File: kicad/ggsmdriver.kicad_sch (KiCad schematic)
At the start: 69 parts, among them J1 DC-005, J2 VIN 9-24V, J3 MOTOR A1 A2 B1 B2, J4 EXP, J5 USB-C, SW1 BOOT, SW2 RESET, U1 STM32G0B1CBT6, U2 TMC2209-LA, U3 TPS54202DDCR, U4 XC6206P332MR, U5 USBLC6-2SC6

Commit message: PCB: hand-laid TMC2209 power stage, no VREF trimmer, real track widths
Motor outputs run 1 mm wide straight to J3 next to the chip (J3 now A2 A1 B1 B2),
sense resistors and VS vias sit at the driver pins, VS caps join through a new
In2.Cu VIN plane, as on the Adafruit breakout. VREF goes to GND since current is
always set over UART. Netclass widths now reach the router. Fully routed, no DRC
errors; fab files regenerated.

Co-Authored-By: Claude Opus 5.5 (1M context) <noreply@anthropic.com>
Claude-Session: https://claude.ai/code/session_01VFhb1Qv7mkaGrgvtw2CS4q
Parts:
- removed R11: 33k, Resistor_SMD:R_0603_1608Metric, symbol Device:R
- removed RV1: 10k current, Potentiometer_SMD:Potentiometer_Bourns_3314J_Vertical, symbol Device:R_Potentiometer_Trim
- J3: value MOTOR A1 A2 B1 B2 -> MOTOR A2 A1 B1 B2
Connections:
- net TMC_VREF is gone; now on net GND: U2.17 (VREF)
- net MOT_A1: now also J3.2 (Pin_2); no longer J3.1 (Pin_1)
- net MOT_A2: now also J3.1 (Pin_1); no longer J3.2 (Pin_2)
- net TMC_SPREAD: no longer U2.7 (SPREAD)
- no-connect marks 31 -> 32
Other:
- moved on the sheet: C16, C17, C18, C19, C20, C21, C22, C23, D4, D5, D6, H1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

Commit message: PCB round 2: no barrel jack, power terminal beside motor terminal, stocked parts
J1 removed; the VIN/GND terminal sits right below the motor terminal on the right
edge. TMC2209-LA-T (C2150710), RALEC 50 mOhm 1206 sense resistors (C154645), red
Basic / green LEDs replace out-of-stock parts. SPREAD pin reconnected (lost in the
previous edit). Fully routed, no DRC errors; fab files regenerated.

Co-Authored-By: Claude Opus 5.5 (1M context) <noreply@anthropic.com>
Claude-Session: https://claude.ai/code/session_01VFhb1Qv7mkaGrgvtw2CS4q
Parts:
- removed J1: DC-005, Connector_BarrelJack:BarrelJack_Horizontal, symbol Connector:Barrel_Jack_Switch
- D2: value PWR green -> PWR red; LCSC C12624 -> C2286
- D3: value STATUS blue -> STATUS green; LCSC C72041 -> C12624
- D4: value STEP yellow -> STEP red; LCSC C2287 -> C2286
- J2: value VIN 9-24V -> VIN 9-24V GND
- R10, R9: LCSC C5185600 -> C154645
- U2: value TMC2209-LA -> TMC2209-LA-T; LCSC C465949 -> C2150710
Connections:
- net TMC_SPREAD: now also U2.7 (SPREAD)
- no-connect marks 32 -> 30
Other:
- note removed: "Power input"
- moved on the sheet: C1, C10, C16, C17, C18, C19, C2, C20, C21, C22, C23, C3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

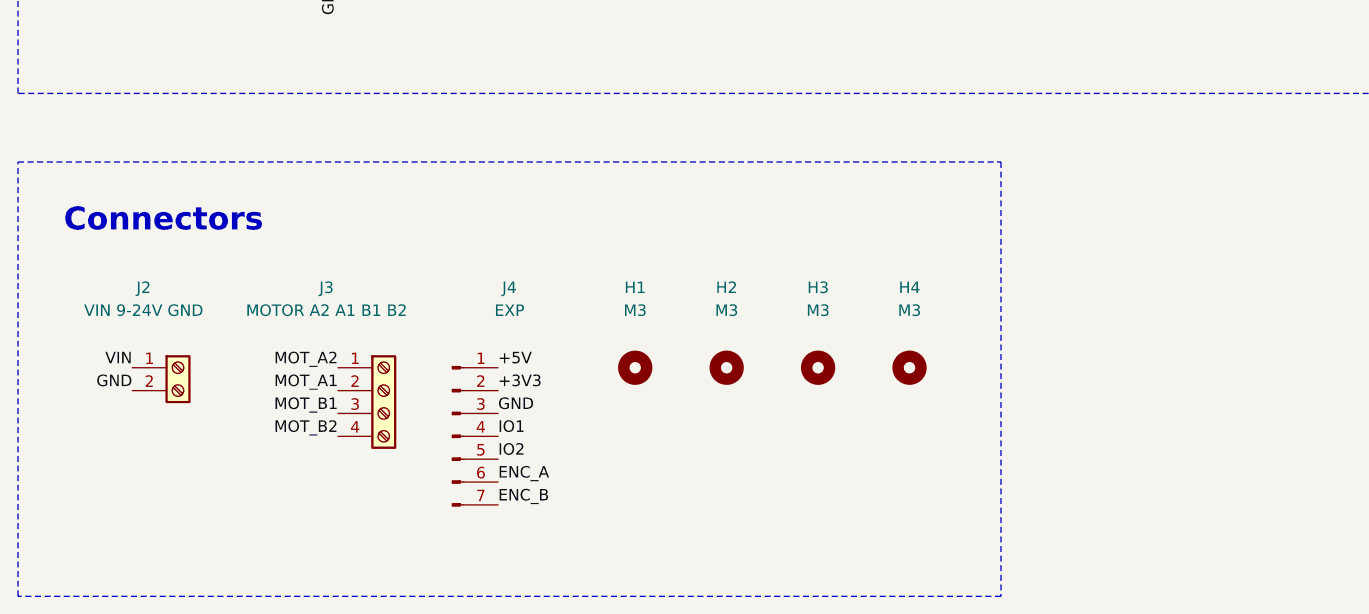
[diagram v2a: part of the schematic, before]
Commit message: PCB: stocked 22 uF cap and three 2-pole terminals
C20 is now Lelon VES220M1HTR-0605 (C176676). The out-of-stock 4-pole motor terminal is
split into two KF350-3.5-2P blocks (J6 coil B, J3 coil A), so power and motor are three
identical 2P blocks along the right edge. Coil B tracks, R10 and C19 moved to make room.
Fully routed, no DRC errors; fab files regenerated.

Co-Authored-By: Claude Opus 5.5 (1M context) <noreply@anthropic.com>
Claude-Session: https://claude.ai/code/session_01VFhb1Qv7mkaGrgvtw2CS4q
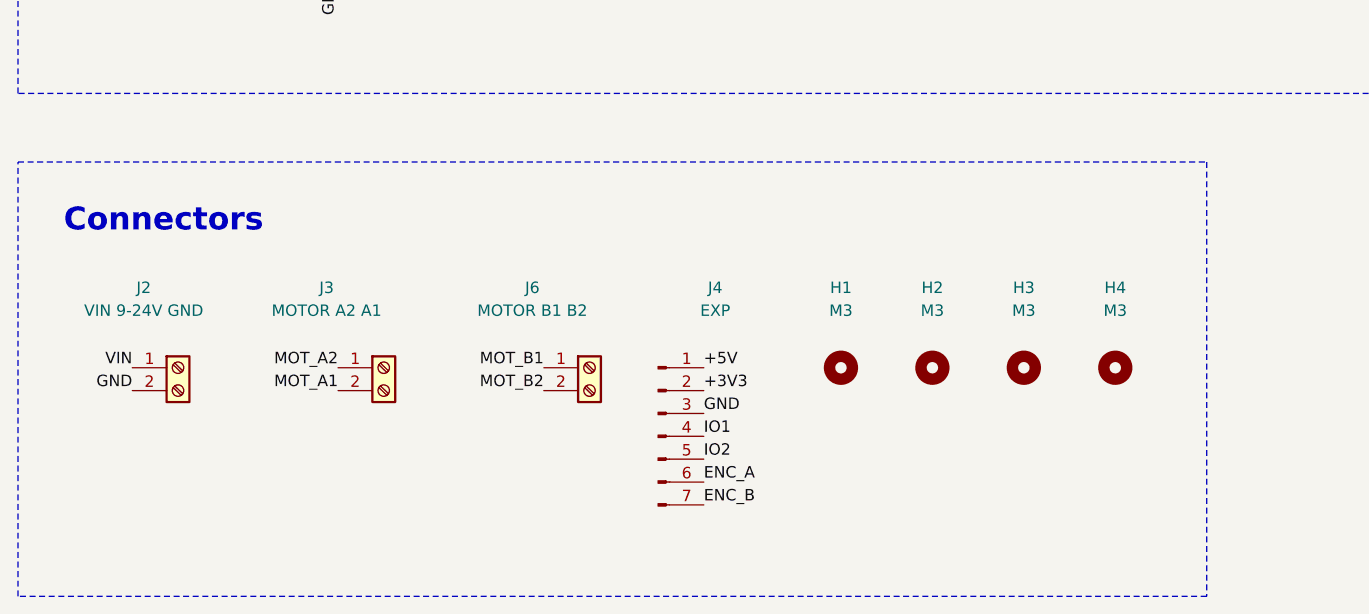
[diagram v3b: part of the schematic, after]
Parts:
- added J6: MOTOR B1 B2, TerminalBlock_Phoenix:TerminalBlock_Phoenix_PT-1,5-2-3.5-H_1x02_P3.50mm_Horizontal, symbol Connector:Screw_Terminal_01x02
- C20: footprint Capacitor_SMD:CP_Elec_6.3x5.9 -> Capacitor_SMD:CP_Elec_6.3x5.4; LCSC C242075 -> C176676
- J3: value MOTOR A2 A1 B1 B2 -> MOTOR A2 A1; footprint TerminalBlock_Phoenix:TerminalBlock_Phoenix_PT-1,5-4-3.5-H_1x04_P3.50mm_Horizontal -> TerminalBlock_Phoenix:TerminalBlock_Phoenix_PT-1,5-2-3.5-H_1x02_P3.50mm_Horizontal; symbol Connector:Screw_Terminal_01x04 -> Connector:Screw_Terminal_01x02; LCSC C42400616 -> C474892
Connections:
- net MOT_B1: now also J6.1 (Pin_1); no longer J3.3 (Pin_3)
- net MOT_B2: now also J6.2 (Pin_2); no longer J3.4 (Pin_4)
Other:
- moved on the sheet: H1, H2, H3, H4, J4
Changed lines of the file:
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@@
   (rectangle
     (start 12.7 246.38)
-    (end 121.92 294.64)
+    (end 144.78 294.64)
     (stroke (width 0) (type dash))
     (fill (type none))
@@
     (property "Reference" "C20" (at 447.04 118.11 0) (effects (font (size 1.27 1.27))))
     (property "Value" "22uF 50V" (at 447.04 120.65 0) (effects (font (size 1.27 1.27))))
-    (property "Footprint" "Capacitor_SMD:CP_Elec_6.3x5.9"
+    (property "Footprint" "Capacitor_SMD:CP_Elec_6.3x5.4"
       (at 447.04 134.62 0)
       (effects (font (size 1.27 1.27)) hide))
     (property "Datasheet" "~" (at 447.04 134.62 0) (effects (font (size 1.27 1.27)) hide))
-    (property "LCSC" "C242075" (at 447.04 134.62 0) (effects (font (size 1.27 1.27)) hide))
+    (property "LCSC" "C176676" (at 447.04 134.62 0) (effects (font (size 1.27 1.27)) hide))
     (pin "1")
     (pin "2")
@@
 )
   (symbol
-    (lib_id "Connector:Screw_Terminal_01x04")
-    (at 53.34 271.78 0)
+    (lib_id "Connector:Screw_Terminal_01x02")
+    (at 53.34 269.24 0)
     (unit 1)
     (in_bom yes)
@@
     (dnp no)
     (property "Reference" "J3" (at 46.99 260.35 0) (effects (font (size 1.27 1.27))))
-    (property "Value" "MOTOR A2 A1 B1 B2" (at 46.99 262.89 0) (effects (font (size 1.27 1.27))))
-    (property "Footprint" "TerminalBlock_Phoenix:TerminalBlock_Phoenix_PT-1,5-4-3.5-H_1x04_P3.50mm_Horizontal"
-      (at 53.34 271.78 0)
-      (effects (font (size 1.27 1.27)) hide))
-    (property "Datasheet" "~" (at 53.34 271.78 0) (effects (font (size 1.27 1.27)) hide))
-    (property "LCSC" "C42400616" (at 53.34 271.78 0) (effects (font (size 1.27 1.27)) hide))
-    (pin "1")
-    (pin "2")
-    (pin "3")
-    (pin "4")
+    (property "Value" "MOTOR A2 A1" (at 46.99 262.89 0) (effects (font (size 1.27 1.27))))
+    (property "Footprint" "TerminalBlock_Phoenix:TerminalBlock_Phoenix_PT-1,5-2-3.5-H_1x02_P3.50mm_Horizontal"
+      (at 53.34 269.24 0)
+      (effects (font (size 1.27 1.27)) hide))
+    (property "Datasheet" "~" (at 53.34 269.24 0) (effects (font (size 1.27 1.27)) hide))
+    (property "LCSC" "C474892" (at 53.34 269.24 0) (effects (font (size 1.27 1.27)) hide))
+    (pin "1")
+    (pin "2")
     (instances
       (project "ggsmdriver"
@@
     (effects (font (size 1.27 1.27)) (justify right bottom))
 )
+  (symbol
+    (lib_id "Connector:Screw_Terminal_01x02")
+    (at 76.2 269.24 0)
+    (unit 1)
+    (in_bom yes)
+    (on_board yes)
+    (dnp no)
+    (property "Reference" "J6" (at 69.85 260.35 0) (effects (font (size 1.27 1.27))))
+    (property "Value" "MOTOR B1 B2" (at 69.85 262.89 0) (effects (font (size 1.27 1.27))))
+    (property "Footprint" "TerminalBlock_Phoenix:TerminalBlock_Phoenix_PT-1,5-2-3.5-H_1x02_P3.50mm_Horizontal"
+      (at 76.2 269.24 0)
+      (effects (font (size 1.27 1.27)) hide))
+    (property "Datasheet" "~" (at 76.2 269.24 0) (effects (font (size 1.27 1.27)) hide))
+    (property "LCSC" "C474892" (at 76.2 269.24 0) (effects (font (size 1.27 1.27)) hide))
+    (pin "1")
+    (pin "2")
+    (instances
+      (project "ggsmdriver"
+        (path "/d2c479e8-b366-5642-b905-795d77a1c823" (reference "J6") (unit 1)))))
   (label "MOT_B1"
-    (at 48.26 274.32 180)
+    (at 71.12 269.24 180)
     (effects (font (size 1.27 1.27)) (justify right bottom))
 )
   (label "MOT_B2"
-    (at 48.26 276.86 180)
+    (at 71.12 271.78 180)
     (effects (font (size 1.27 1.27)) (justify right bottom))
 )
   (symbol
     (lib_id "Connector:Conn_01x07_Pin")
-    (at 60.96 276.86 0)
-    (unit 1)
-    (in_bom yes)
-    (on_board yes)
-    (dnp no)
-    (property "Reference" "J4" (at 67.31 260.35 0) (effects (font (size 1.27 1.27))))
-    (property "Value" "EXP" (at 67.31 262.89 0) (effects (font (size 1.27 1.27))))
+    (at 83.82 276.86 0)
+    (unit 1)
+    (in_bom yes)
+    (on_board yes)
+    (dnp no)
+    (property "Reference" "J4" (at 90.17 260.35 0) (effects (font (size 1.27 1.27))))
+    (property "Value" "EXP" (at 90.17 262.89 0) (effects (font (size 1.27 1.27))))
     (property "Footprint" "Connector_PinHeader_2.54mm:PinHeader_1x07_P2.54mm_Vertical"
-      (at 60.96 276.86 0)
-      (effects (font (size 1.27 1.27)) hide))
-    (property "Datasheet" "~" (at 60.96 276.86 0) (effects (font (size 1.27 1.27)) hide))
-    (property "LCSC" "C492406" (at 60.96 276.86 0) (effects (font (size 1.27 1.27)) hide))
+      (at 83.82 276.86 0)
+      (effects (font (size 1.27 1.27)) hide))
+    (property "Datasheet" "~" (at 83.82 276.86 0) (effects (font (size 1.27 1.27)) hide))
+    (property "LCSC" "C492406" (at 83.82 276.86 0) (effects (font (size 1.27 1.27)) hide))
     (pin "1")
     (pin "2")
@@
         (path "/d2c479e8-b366-5642-b905-795d77a1c823" (reference "J4") (unit 1)))))
   (label "+5V"
-    (at 66.04 269.24 0)
+    (at 88.9 269.24 0)
     (effects (font (size 1.27 1.27)) (justify left bottom))
 )
   (label "+3V3"
-    (at 66.04 271.78 0)
-    (effects (font (size 1.27 1.27)) (justify left bottom))
-)
-  (label "GND"
-    (at 66.04 274.32 0)
+    (at 88.9 271.78 0)
+    (effects (font (size 1.27 1.27)) (justify left bottom))
+)
+  (label "GND"
+    (at 88.9 274.32 0)
     (effects (font (size 1.27 1.27)) (justify left bottom))
 )
   (label "IO1"
-    (at 66.04 276.86 0)
+    (at 88.9 276.86 0)
     (effects (font (size 1.27 1.27)) (justify left bottom))
 )
   (label "IO2"
-    (at 66.04 279.4 0)
+    (at 88.9 279.4 0)
     (effects (font (size 1.27 1.27)) (justify left bottom))
 )
   (label "ENC_A"
-    (at 66.04 281.94 0)
+    (at 88.9 281.94 0)
     (effects (font (size 1.27 1.27)) (justify left bottom))
 )
   (label "ENC_B"
-    (at 66.04 284.48 0)
+    (at 88.9 284.48 0)
     (effects (font (size 1.27 1.27)) (justify left bottom))
 )
   (symbol
     (lib_id "Mechanical:MountingHole")
-    (at 81.28 269.24 0)
-    (unit 1)
-    (in_bom yes)
-    (on_board yes)
-    (dnp no)
-    (property "Reference" "H1" (at 81.28 260.35 0) (effects (font (size 1.27 1.27))))
-    (property "Value" "M3" (at 81.28 262.89 0) (effects (font (size 1.27 1.27))))
+    (at 104.14 269.24 0)
+    (unit 1)
+    (in_bom yes)
+    (on_board yes)
+    (dnp no)
+    (property "Reference" "H1" (at 104.14 260.35 0) (effects (font (size 1.27 1.27))))
+    (property "Value" "M3" (at 104.14 262.89 0) (effects (font (size 1.27 1.27))))
     (property "Footprint" "MountingHole:MountingHole_3.2mm_M3"
-      (at 81.28 269.24 0)
-      (effects (font (size 1.27 1.27)) hide))
-    (property "Datasheet" "~" (at 81.28 269.24 0) (effects (font (size 1.27 1.27)) hide))
+      (at 104.14 269.24 0)
+      (effects (font (size 1.27 1.27)) hide))
+    (property "Datasheet" "~" (at 104.14 269.24 0) (effects (font (size 1.27 1.27)) hide))
     (instances
       (project "ggsmdriver"
@@
   (symbol
     (lib_id "Mechanical:MountingHole")
-    (at 91.44 269.24 0)
-    (unit 1)
-    (in_bom yes)
-    (on_board yes)
-    (dnp no)
-    (property "Reference" "H2" (at 91.44 260.35 0) (effects (font (size 1.27 1.27))))
-    (property "Value" "M3" (at 91.44 262.89 0) (effects (font (size 1.27 1.27))))
+    (at 114.3 269.24 0)
+    (unit 1)
+    (in_bom yes)
+    (on_board yes)
+    (dnp no)
+    (property "Reference" "H2" (at 114.3 260.35 0) (effects (font (size 1.27 1.27))))
+    (property "Value" "M3" (at 114.3 262.89 0) (effects (font (size 1.27 1.27))))
     (property "Footprint" "MountingHole:MountingHole_3.2mm_M3"
-      (at 91.44 269.24 0)
-      (effects (font (size 1.27 1.27)) hide))
-    (property "Datasheet" "~" (at 91.44 269.24 0) (effects (font (size 1.27 1.27)) hide))
+      (at 114.3 269.24 0)
+      (effects (font (size 1.27 1.27)) hide))
+    (property "Datasheet" "~" (at 114.3 269.24 0) (effects (font (size 1.27 1.27)) hide))
     (instances
       (project "ggsmdriver"
@@
   (symbol
     (lib_id "Mechanical:MountingHole")
-    (at 101.6 269.24 0)
-    (unit 1)
-    (in_bom yes)
-    (on_board yes)
-    (dnp no)
-    (property "Reference" "H3" (at 101.6 260.35 0) (effects (font (size 1.27 1.27))))
-    (property "Value" "M3" (at 101.6 262.89 0) (effects (font (size 1.27 1.27))))
+    (at 124.46 269.24 0)
+    (unit 1)
+    (in_bom yes)
+    (on_board yes)
+    (dnp no)
+    (property "Reference" "H3" (at 124.46 260.35 0) (effects (font (size 1.27 1.27))))
+    (property "Value" "M3" (at 124.46 262.89 0) (effects (font (size 1.27 1.27))))
     (property "Footprint" "MountingHole:MountingHole_3.2mm_M3"
-      (at 101.6 269.24 0)
-      (effects (font (size 1.27 1.27)) hide))
-    (property "Datasheet" "~" (at 101.6 269.24 0) (effects (font (size 1.27 1.27)) hide))
+      (at 124.46 269.24 0)
+      (effects (font (size 1.27 1.27)) hide))
+    (property "Datasheet" "~" (at 124.46 269.24 0) (effects (font (size 1.27 1.27)) hide))
     (instances
       (project "ggsmdriver"
@@
   (symbol
     (lib_id "Mechanical:MountingHole")
-    (at 111.76 269.24 0)
-    (unit 1)
-    (in_bom yes)
-    (on_board yes)
-    (dnp no)
-    (property "Reference" "H4" (at 111.76 260.35 0) (effects (font (size 1.27 1.27))))
-    (property "Value" "M3" (at 111.76 262.89 0) (effects (font (size 1.27 1.27))))
+    (at 134.62 269.24 0)
+    (unit 1)
+    (in_bom yes)
+    (on_board yes)
+    (dnp no)
+    (property "Reference" "H4" (at 134.62 260.35 0) (effects (font (size 1.27 1.27))))
+    (property "Value" "M3" (at 134.62 262.89 0) (effects (font (size 1.27 1.27))))
     (property "Footprint" "MountingHole:MountingHole_3.2mm_M3"
-      (at 111.76 269.24 0)
-      (effects (font (size 1.27 1.27)) hide))
-    (property "Datasheet" "~" (at 111.76 269.24 0) (effects (font (size 1.27 1.27)) hide))
-    (instances
-      (project "ggsmdriver"
+      (at 134.62 269.24 0)
+      (effects (font (size 1.27 1.27)) hide))
+    (property "Datasheet" "~" (at 134.62 269.24 0) (effects (font (size 1.27 1.27)) hide))
+    (instances
+      (project "ggsmdriver"

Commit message: PCB: one 6-pole 2.54 mm terminal for power and motor
KF128-2.54-6P (C474924) replaces the three 3.5 mm 2-pole blocks, as on the Adafruit
breakout. Motor tracks re-laid to the 2.54 mm pins. Fully routed, no DRC errors; fab files
regenerated.

Co-Authored-By: Claude Opus 5.5 (1M context) <noreply@anthropic.com>
Claude-Session: https://claude.ai/code/session_01VFhb1Qv7mkaGrgvtw2CS4q
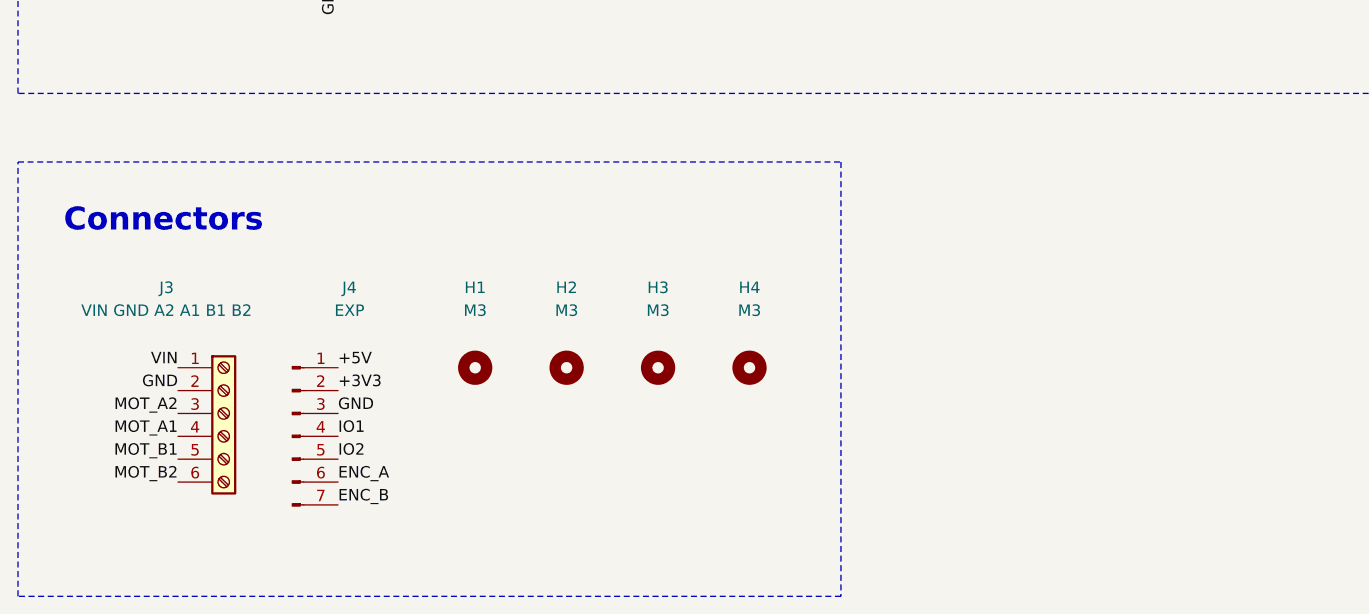
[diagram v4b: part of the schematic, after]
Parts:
- removed J2: VIN 9-24V GND, TerminalBlock_Phoenix:TerminalBlock_Phoenix_PT-1,5-2-3.5-H_1x02_P3.50mm_Horizontal, symbol Connector:Screw_Terminal_01x02
- removed J6: MOTOR B1 B2, TerminalBlock_Phoenix:TerminalBlock_Phoenix_PT-1,5-2-3.5-H_1x02_P3.50mm_Horizontal, symbol Connector:Screw_Terminal_01x02
- J3: value MOTOR A2 A1 -> VIN GND A2 A1 B1 B2; footprint TerminalBlock_Phoenix:TerminalBlock_Phoenix_PT-1,5-2-3.5-H_1x02_P3.50mm_Horizontal -> TerminalBlock_Phoenix:TerminalBlock_Phoenix_MPT-0,5-6-2.54_1x06_P2.54mm_Horizontal; symbol Connector:Screw_Terminal_01x02 -> Connector:Screw_Terminal_01x06; LCSC C474892 -> C474924
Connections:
- net GND: now also J3.2 (Pin_2)
- net MOT_A1: now also J3.4 (Pin_4); no longer J3.2 (Pin_2)
- net MOT_A2: now also J3.3 (Pin_3); no longer J3.1 (Pin_1)
- net MOT_B1: now also J3.5 (Pin_5)
- net MOT_B2: now also J3.6 (Pin_6)
- net VIN: now also J3.1 (Pin_1)
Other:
- moved on the sheet: H1, H2, H3, H4, J4
